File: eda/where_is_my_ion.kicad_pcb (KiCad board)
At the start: 4 copper layers, 88 x 163 mm, 156 parts, among them J1 USB_C_Receptacle_USB2.0_16P, Q1 L8050QLT1G, Q2 L8050QLT1G, SW1 SW_MCU_RESET, SW2 FORCE_REFRESH, SW3 NEXT_TRAIN, SW4 SW_BOOT_SEL, U1 CP2102N-Axx-xQFN28, U2 TLC59116IPWR, U3 TLC59116IPWR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

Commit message: almost done, just silkscreen now
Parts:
- removed TP6: TestPoint, TestPoint:TestPoint_Pad_D2.0mm
- moved TP7 9.75 mm to (92.2, 156.2)
- moved TP10 5.00 mm to (87.0, 156.2)
- moved D83 0.60 mm to (94.2, 175.4)
- moved D84 0.45 mm to (90.8, 175.3)
- moved U6 0.40 mm to (124.0, 156.7)
- moved J1 0.38 mm to (92.4, 182.7)
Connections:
- TP7 pad 1: /IO1_SW -> /IO10
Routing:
- net +3V3: track 84.0 -> 262.6 mm, vias 15 -> 53
- net GND: track 122.8 -> 168.2 mm, vias 29 -> 37
- net /IO10: track 0.00 -> 29.5 mm, vias 0 -> 1
- net /VBUS: track 14.0 -> 19.9 mm, vias 0 -> 2
- net /CHIP_PU: track 60.8 -> 63.6 mm
- net /IO6_SCL: track 312.6 -> 310.4 mm, vias 11 -> 10
- net /IO4_~{RESET}: track 311.0 -> 313.1 mm, vias 11 -> 10
- net /STN_REV_MILL: track 52.6 -> 54.3 mm
- net /IO5_SDA: track 334.9 -> 333.3 mm, vias 11 -> 10
- net /IO9: track 78.7 -> 77.4 mm
- net /STN_CONESTOGA: track 64.7 -> 65.4 mm
- net /STN_REV_UW: track 29.1 -> 29.7 mm
- net /~{DTR}: track 54.6 -> 55.1 mm

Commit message: comit:wq
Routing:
- net /STN_CONESTOGA: track 65.4 -> 66.9 mm
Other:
- board text added: "ALLEN"
- board text added: "BLOCK LINE"
- board text added: "BORDEN"
- board text added: "CENTRAL"
- board text added: "CONESTOGA"
- board text added: "FAIRWAY"
- board text added: "GRH"
- board text added: "KITCHENER CITY HALL"
- board text added: "KITCHENER MARKET"
- board text added: "LAURIER-WATERLOO PARK"
- board text added: "MILL"
- board text added: "NORTHFIELD"
- board text added: "QUEEN"
- board text added: "RSRCH & TECH"
- board text added: "UNIV. OF WATERLOO"
- board text added: "VICTORIA"
- board text added: "WATERLOO PUBLIC SQ"
- board text added: "WILLIs WAY"

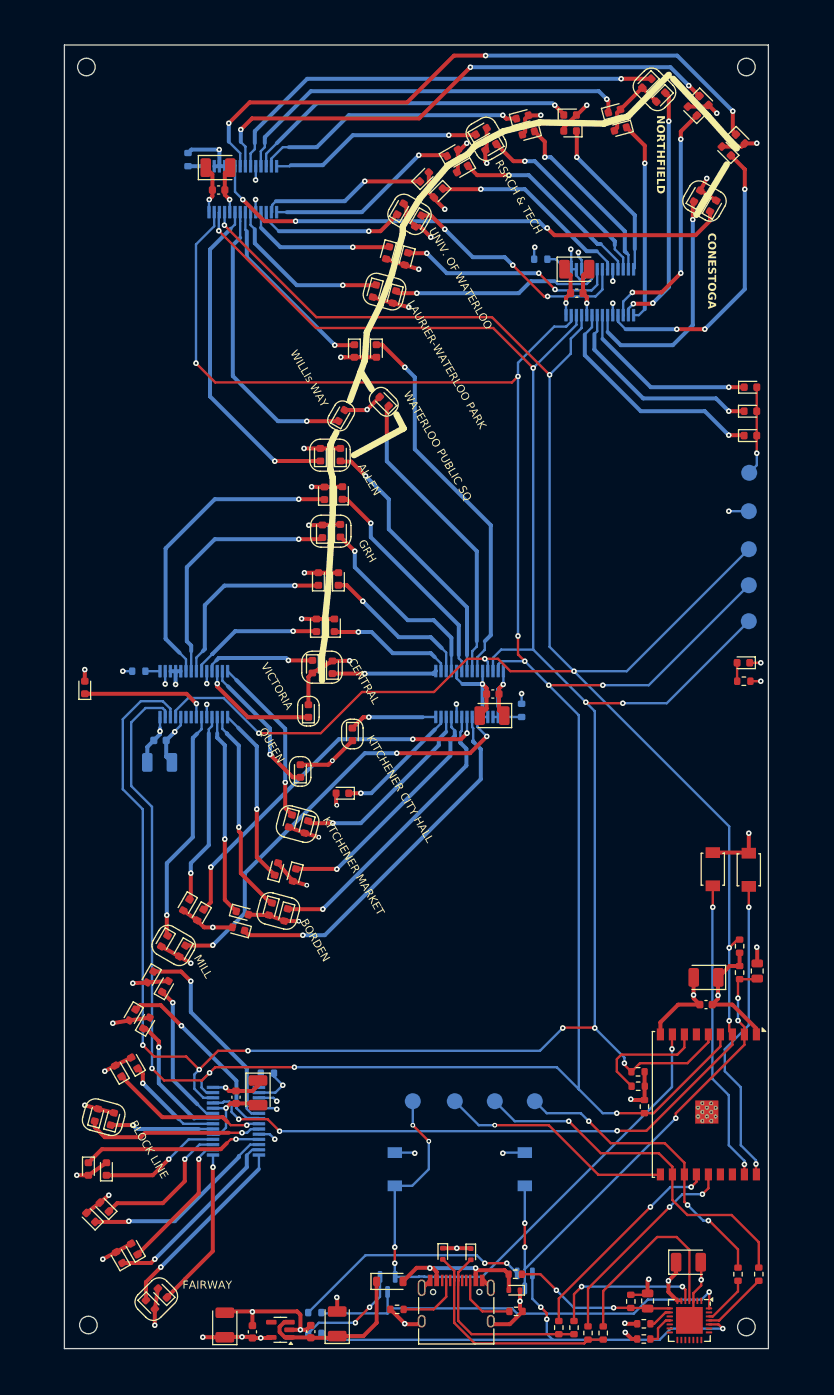
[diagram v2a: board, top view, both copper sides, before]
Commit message: more silk
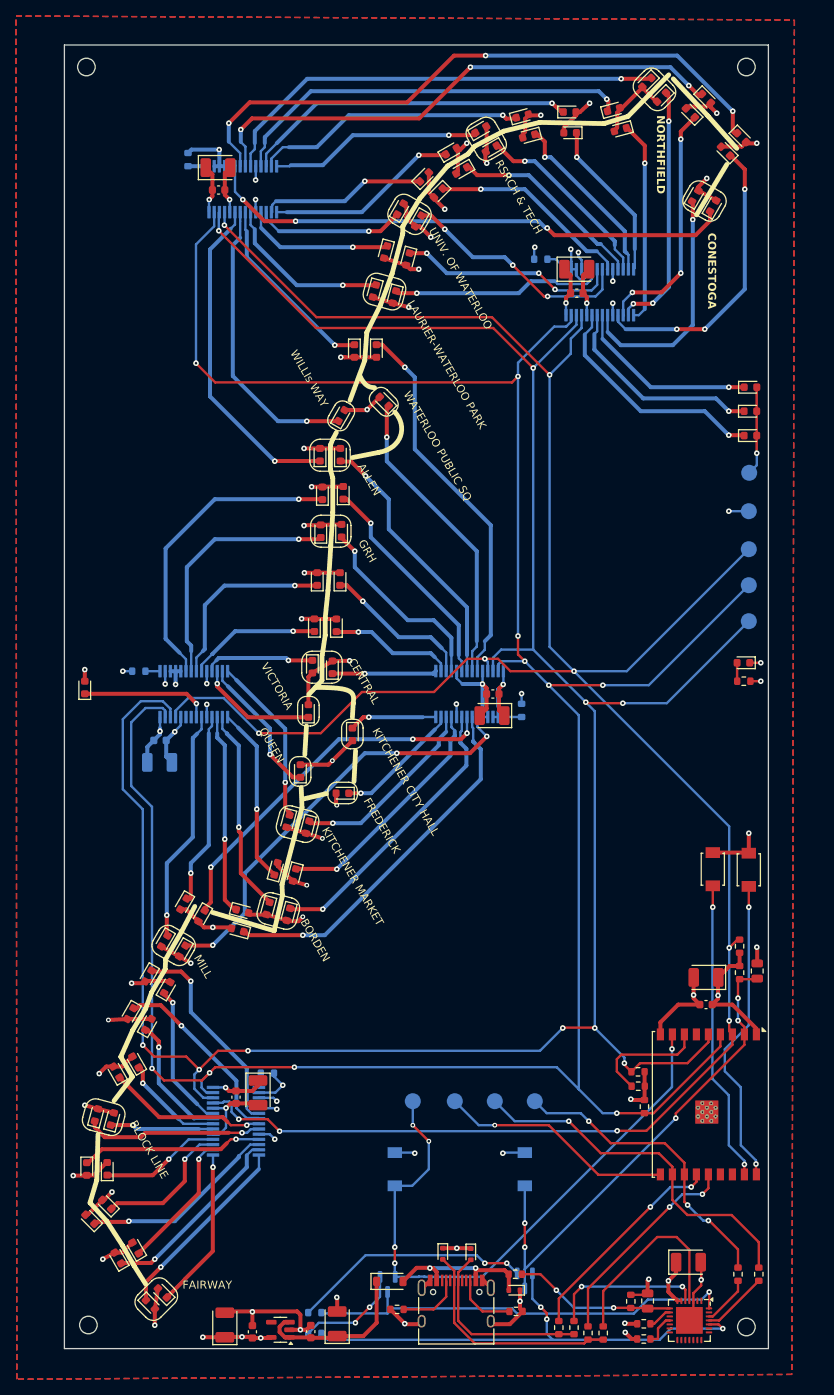
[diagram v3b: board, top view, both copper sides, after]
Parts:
- moved D30 0.44 mm to (48.8, 169.2)
- moved D6 0.41 mm to (123.7, 30.9)
- moved D3 0.38 mm to (106.6, 32.6)
- moved D65 0.38 mm to (101.5, 35.6)
- moved D51 0.37 mm to (58.4, 131.6)
- moved D78 0.34 mm to (121.7, 32.7)
- moved D53 0.31 mm to (68.9, 132.2)
- moved D26 0.31 mm to (54.0, 146.7)
- moved D15 0.31 mm to (51.7, 145.3)
- moved D45 0.30 mm to (71.5, 132.9)
- moved D33 0.30 mm to (71.4, 121.2)
- moved D25 0.28 mm to (56.3, 142.1)
- moved D14 0.28 mm to (50.0, 152.6)
- moved D16 0.28 mm to (54.0, 140.6)
- moved D21 0.28 mm to (83.6, 50.1)
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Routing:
- net +3V3: track 262.6 -> 276.1 mm
- added copper zone on B.Cu, net GND
- added copper zone on F.Cu, net GND
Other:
- board text added: "FREDERICK"
